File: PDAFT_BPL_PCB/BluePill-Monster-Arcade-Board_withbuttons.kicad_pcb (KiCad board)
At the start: 2 copper layers, 91.7 x 65.8 mm, 19 parts, among them J1 Conn_01x02, J2 Conn_01x04, U1 YAAJ_BluePill_Part_Like, U2 ProMicro, U3 ULN2003, U4 ULN2003

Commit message: bluepill update
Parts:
- moved Arduino_power1 55.5 mm to (176.9, 114.3), turned to 90 degrees
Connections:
- Arduino_power1 pad 1: Net-(Arduino_power1-Pad1) -> Net-(Circle1-Pad1)
- Circle1 pad 1: Net-(Arduino_power1-Pad1) -> Net-(Circle1-Pad1)
- Cross1 pad 1: Net-(Arduino_power1-Pad1) -> Net-(Circle1-Pad1)
- J1 pad 1: Net-(Arduino_power1-Pad1) -> Net-(Arduino_power1-Pad2)
- J2 pad 1: Net-(Arduino_power1-Pad1) -> Net-(Arduino_power1-Pad2)
- Square1 pad 1: Net-(Arduino_power1-Pad1) -> Net-(Circle1-Pad1)
- Triangle1 pad 1: Net-(Arduino_power1-Pad1) -> Net-(Circle1-Pad1)
- U1 pad 18: Net-(Arduino_power1-Pad1) -> Net-(Arduino_power1-Pad2)
- U2 pad 21: Net-(Arduino_power1-Pad2) -> Net-(Circle1-Pad1)
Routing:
- net Net-(Arduino_power1-Pad1): track 159.1 -> 0.00 mm
- net Net-(Circle1-Pad1): track 0.00 -> 120.8 mm
- net Net-(Arduino_power1-Pad2): track 6.10 -> 44.9 mm

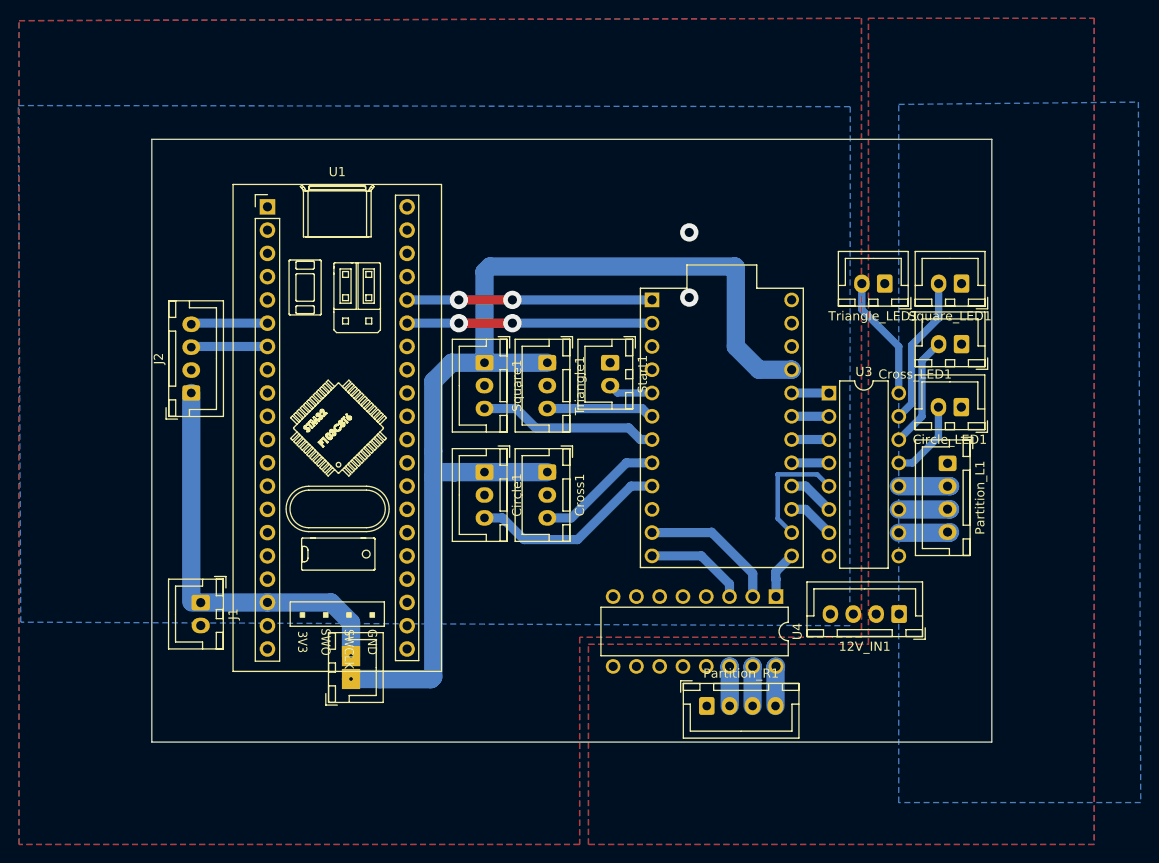
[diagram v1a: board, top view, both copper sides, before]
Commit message: Update of bluepill moster with buttons to order on JLCPCB
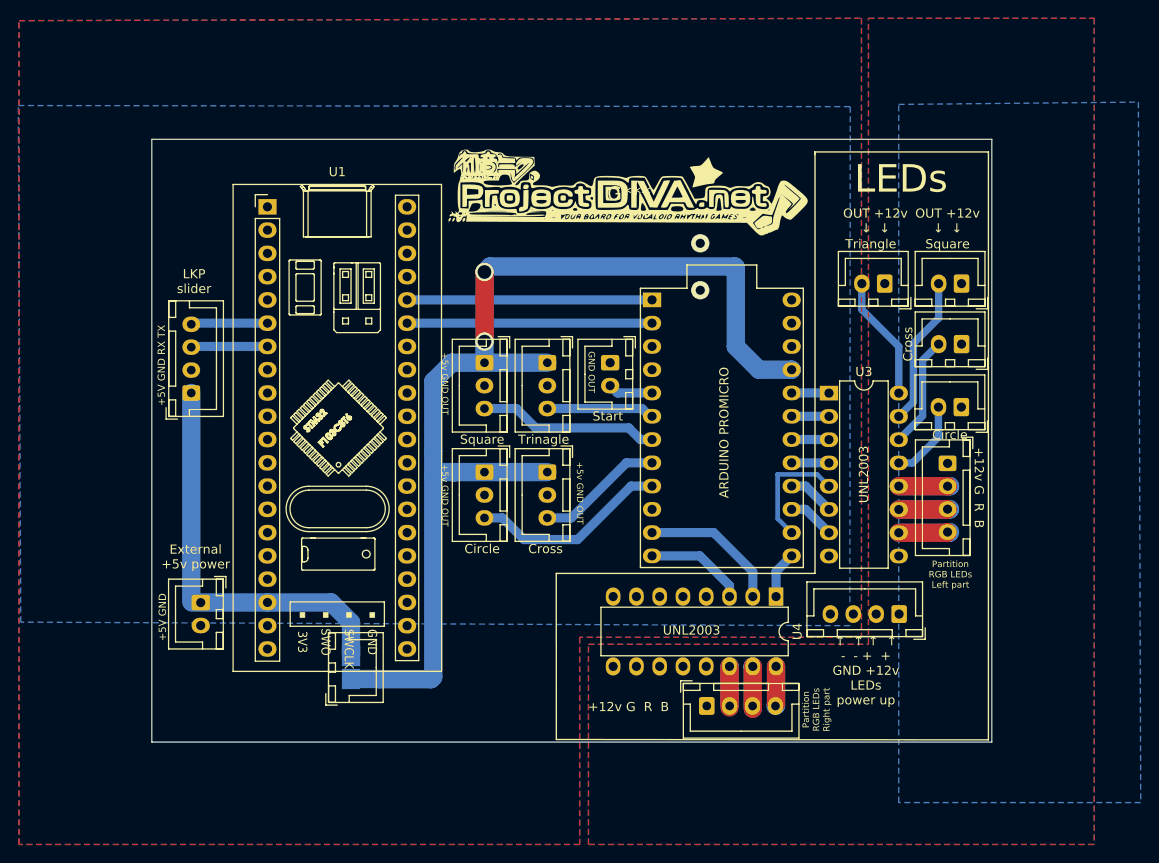
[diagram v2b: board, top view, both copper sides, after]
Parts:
- added G***: LOGO, logos:projectdivanet, F.Cu at (207.3, 61.3)
- added G***: LOGO, logos:projectdiva_logo, B.Cu at (212.0, 63.9)
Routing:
- net Net-(Partition_L1-Pad4): track 5.63 -> 11.0 mm
- net Net-(Partition_L1-Pad3): track 5.61 -> 10.9 mm
- net Net-(Partition_L1-Pad2): track 5.60 -> 10.9 mm
- net Net-(Partition_R1-Pad3): track 4.33 -> 8.97 mm
- net Net-(Partition_R1-Pad2): track 4.33 -> 8.81 mm
- net Net-(Partition_R1-Pad4): track 4.34 -> 8.38 mm
- net Net-(Arduino_power1-Pad1): vias 0 -> 2
- net Net-(U1-Pad36): vias 2 -> 0
- net Net-(U1-Pad35): vias 2 -> 0
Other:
- board text added: "+12v G R B"
- board text added: "+12v OUT ↓ ↓"
- board text added: "+5V GND"
- board text added: "+5V GND RX TX"
- board text added: "+5v GND OUT"
- board text added: "ARDUINO PROMICRO"
- board text added: "B R G +12v"
- board text added: "Circle"
- board text added: "Cross"
- board text added: "External +5v power"
- board text added: "GND +5V"
- board text added: "GND OUT"
- board text added: "LEDs"
- board text added: "LKP slider"
- board text added: "OUT +12v ↓ ↓"
- board text added: "OUT GND"
- board text added: "OUT GND +5v"
- board text added: "Partition RGB LEDs Left part"
- board text added: "Partition RGB LEDs Right part"
- board text added: "Project DIVA Arcade Future Tone controller with slider and partition/button LEDs support by steelpuxnastik (projectdiva.net)"
- board text added: "Short if you need external +5V power up from one source (be sure that you use USB-cable without +5v line)"
- board text added: "Square"
- board text added: "Start"
- board text added: "TX RX GND +5v"
- board text added: "Triangle"
- board text added: "Trinagle"
- board text added: "UNL2003"
- board text added: "↑ ↑ ↑ ↑ + + - - +12v GND LEDs power up"
- board text added: "↑ ↑ ↑ ↑ - - + + GND +12v LEDs power up"
